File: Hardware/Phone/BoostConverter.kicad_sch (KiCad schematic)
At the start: 9 parts

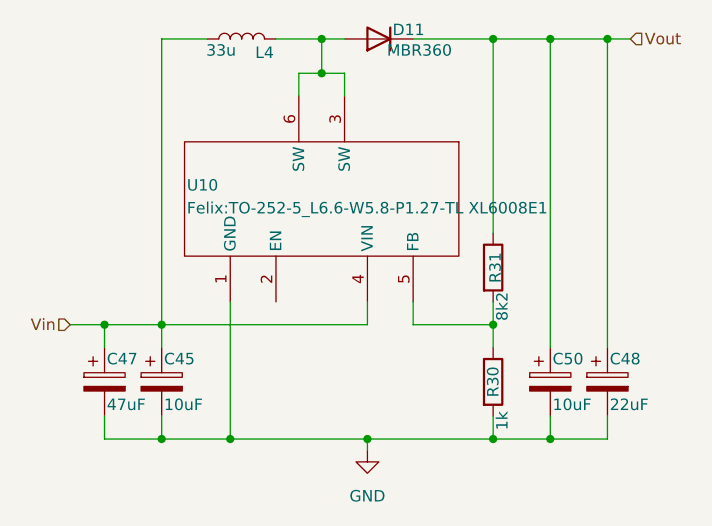
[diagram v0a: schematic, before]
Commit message: added doku. Abendoning Projekt
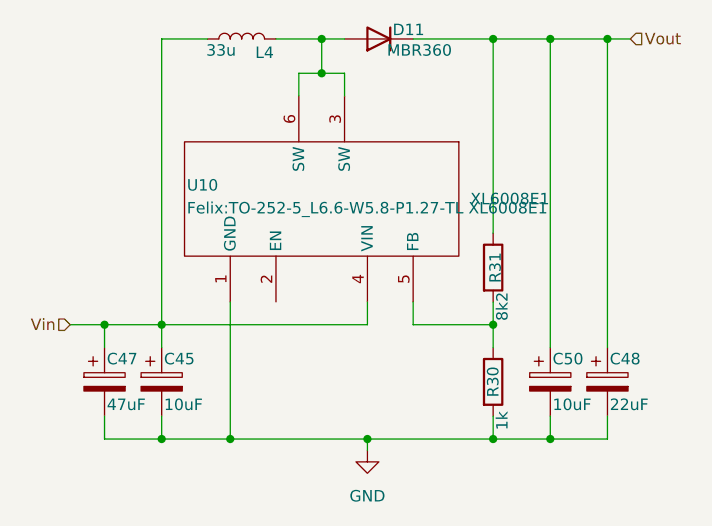
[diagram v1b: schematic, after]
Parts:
- U10: value ~ -> XL6008E1
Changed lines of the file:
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@@
 			)
 		)
-		(property "Value" "~"
+		(property "Value" "XL6008E1"
 			(at 135.89 109.22 90)
 			(effects
